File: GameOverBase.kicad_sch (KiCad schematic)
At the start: 51 parts, among them J1 USB_C_Receptacle_USB2.0, J2 Serial Port, J3 add-on conn, Q1 PMN48XP, SW1 SW_DIP_x08, SW2 boot, SW3 Reset, U1 ESP32-WROOM-E, U2 4021, U3 MCP73831-2ACI-OT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

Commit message: Adds footprint for CTS 219-8LPST DIP switches
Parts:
- SW2, SW3: footprint (none) -> GameOver:TXGA_FFC05036-24SBD113W5M_1x24_P0.50mm_Horizontal
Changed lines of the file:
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@@
       (effects (font (size 1.27 1.27)))
     )
-    (property "Footprint" "" (id 2) (at 224.79 146.05 0)
+    (property "Footprint" "GameOver:TXGA_FFC05036-24SBD113W5M_1x24_P0.50mm_Horizontal" (id 2) (at 224.79 146.05 0)
       (effects (font (size 1.27 1.27)) hide)
     )
@@
       (effects (font (size 1.27 1.27)))
     )
-    (property "Footprint" "" (id 2) (at 207.01 146.05 0)
+    (property "Footprint" "GameOver:TXGA_FFC05036-24SBD113W5M_1x24_P0.50mm_Horizontal" (id 2) (at 207.01 146.05 0)
       (effects (font (size 1.27 1.27)) hide)
     )
@@
     )
     (path "/407d0ffb-4748-48d0-84ea-57fc2a5b2510"
-      (reference "SW1") (unit 1) (value "SW_DIP_x08") (footprint "")
+      (reference "SW1") (unit 1) (value "SW_DIP_x08") (footprint "GameOver:DIP-16_CTS_219-8LPST")
     )
     (path "/fbfbda5b-3f1a-4559-9c00-adeb4e1f53ab"

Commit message: Fixes footprint association for both tactile switches
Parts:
- SW1: footprint (none) -> GameOver:DIP-16_CTS_219-8LPST
- SW2, SW3: footprint GameOver:TXGA_FFC05036-24SBD113W5M_1x24_P0.50mm_Horizontal -> (none)
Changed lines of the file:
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@@
       (effects (font (size 1.27 1.27)))
     )
-    (property "Footprint" "GameOver:TXGA_FFC05036-24SBD113W5M_1x24_P0.50mm_Horizontal" (id 2) (at 224.79 146.05 0)
+    (property "Footprint" "" (id 2) (at 224.79 146.05 0)
       (effects (font (size 1.27 1.27)) hide)
     )
@@
       (effects (font (size 1.27 1.27)))
     )
-    (property "Footprint" "" (id 2) (at 121.92 158.75 0)
+    (property "Footprint" "GameOver:DIP-16_CTS_219-8LPST" (id 2) (at 121.92 158.75 0)
       (effects (font (size 1.27 1.27)) hide)
     )
@@
       (effects (font (size 1.27 1.27)))
     )
-    (property "Footprint" "GameOver:TXGA_FFC05036-24SBD113W5M_1x24_P0.50mm_Horizontal" (id 2) (at 207.01 146.05 0)
+    (property "Footprint" "" (id 2) (at 207.01 146.05 0)
       (effects (font (size 1.27 1.27)) hide)
     )
@@
     )
     (path "/fbfbda5b-3f1a-4559-9c00-adeb4e1f53ab"
-      (reference "SW2") (unit 1) (value "boot") (footprint "GameOver:TXGA_FFC05036-24SBD113W5M_1x24_P0.50mm_Horizontal")
+      (reference "SW2") (unit 1) (value "boot") (footprint "GameOver:SW_Tactile_SPST_SOFNG_TS-1814")
     )
     (path "/127be547-9fbb-4f55-a1d1-e12de114ea72"
-      (reference "SW3") (unit 1) (value "Reset") (footprint "GameOver:TXGA_FFC05036-24SBD113W5M_1x24_P0.50mm_Horizontal")
+      (reference "SW3") (unit 1) (value "Reset") (footprint "GameOver:SW_Tactile_SPST_SOFNG_TS-1814")
     )
     (path "/7e6285e9-8fc0-49bf-b49b-a6df46890238"

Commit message: Uses tag-connect TC2030-FP footprint for serial connection to uC
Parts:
- SW2, SW3: footprint (none) -> GameOver:SW_Tactile_SPST_SOFNG_TS-1814
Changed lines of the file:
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@@
       (effects (font (size 1.27 1.27)))
     )
-    (property "Footprint" "" (id 2) (at 224.79 146.05 0)
+    (property "Footprint" "GameOver:SW_Tactile_SPST_SOFNG_TS-1814" (id 2) (at 224.79 146.05 0)
       (effects (font (size 1.27 1.27)) hide)
     )
@@
       (effects (font (size 1.27 1.27)))
     )
-    (property "Footprint" "" (id 2) (at 207.01 146.05 0)
+    (property "Footprint" "GameOver:SW_Tactile_SPST_SOFNG_TS-1814" (id 2) (at 207.01 146.05 0)
       (effects (font (size 1.27 1.27)) hide)
     )
@@
     )
     (path "/a4a4a9b2-b00e-4de8-947c-82cb95b02a26"
-      (reference "J2") (unit 1) (value "Serial Port") (footprint "")
+      (reference "J2") (unit 1) (value "Serial Port") (footprint "Connector:Tag-Connect_TC2030-IDC-FP_2x03_P1.27mm_Vertical")
     )
     (path "/b96389fd-4b84-4e6a-b451-5d6147af997a"

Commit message: Fixes footprint for 4021B
It actually uses TSSOP16 without thermal pads
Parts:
- J2: footprint (none) -> Connector:Tag-Connect_TC2030-IDC-FP_2x03_P1.27mm_Vertical
- U2: footprint Package_SO:TSSOP-16-1EP_4.4x5mm_P0.65mm -> (none)
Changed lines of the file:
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@@
       (effects (font (size 1.27 1.27)) (justify left))
     )
-    (property "Footprint" "Package_SO:TSSOP-16-1EP_4.4x5mm_P0.65mm" (id 2) (at 165.1 147.32 0)
+    (property "Footprint" "" (id 2) (at 165.1 147.32 0)
       (effects (font (size 1.27 1.27)) hide)
     )
@@
       (effects (font (size 1.27 1.27)))
     )
-    (property "Footprint" "" (id 2) (at 49.53 179.07 0)
+    (property "Footprint" "Connector:Tag-Connect_TC2030-IDC-FP_2x03_P1.27mm_Vertical" (id 2) (at 49.53 179.07 0)
       (effects (font (size 1.27 1.27)) hide)
     )
@@
     )
     (path "/317e242a-fc94-41fd-8e86-30d2c1650759"
-      (reference "U2") (unit 1) (value "4021") (footprint "Package_SO:TSSOP-16-1EP_4.4x5mm_P0.65mm")
+      (reference "U2") (unit 1) (value "4021") (footprint "Package_SO:TSSOP-16_4.4x5mm_P0.65mm")
     )
     (path "/e16932c6-4644-4ca2-b59a-6a89b09e35e0"

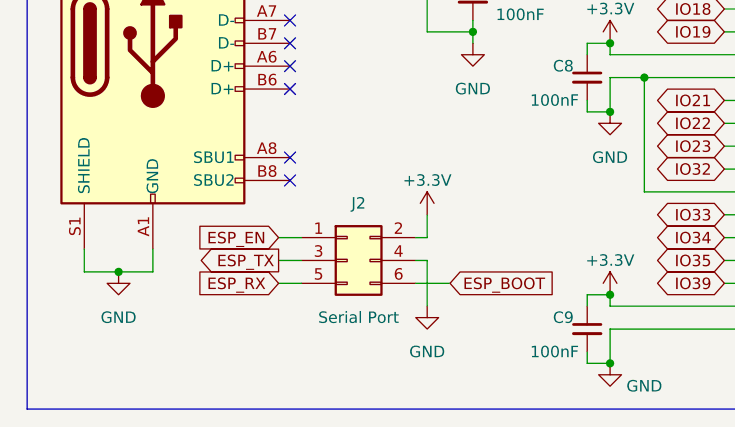
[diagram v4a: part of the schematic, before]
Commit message: Adds solder jumpers to the TX/RX lines
This will make it easier to bodge the PCB in case we mix the lines up.
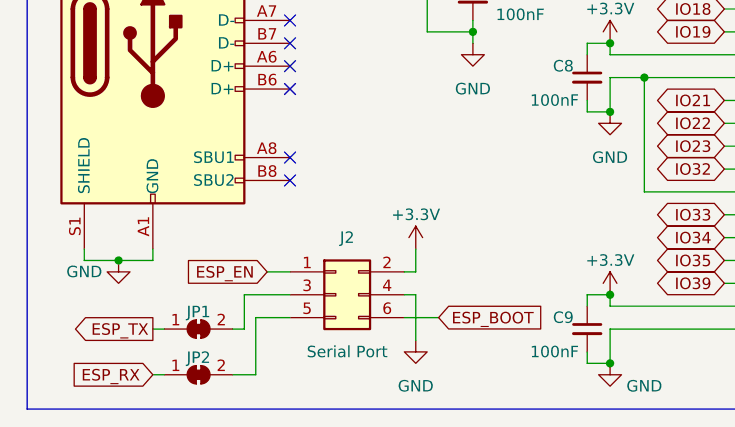
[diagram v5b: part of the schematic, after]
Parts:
- added JP1: (no value), symbol Jumper:SolderJumper_2_Bridged
- added JP2: ~, symbol Jumper:SolderJumper_2_Bridged
- U2: footprint (none) -> Package_SO:TSSOP-16_4.4x5mm_P0.65mm
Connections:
- net ESP_RX: now also JP2.1 (A); no longer J2.5 (Pin_5)
- net ESP_TX: now also JP1.1 (A); no longer J2.3 (Pin_3)
- new net: J2.3 (Pin_3), JP1.2 (B)
- new net: J2.5 (Pin_5), JP2.2 (B)
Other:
- moved on the sheet: J2

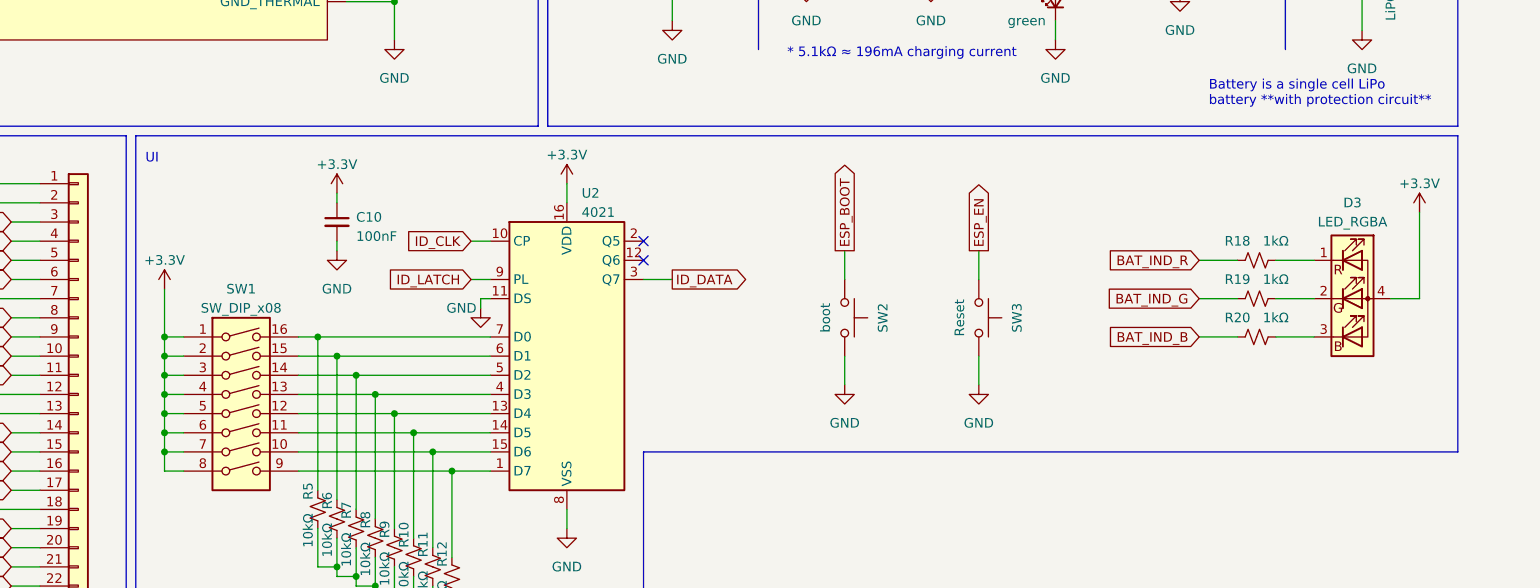
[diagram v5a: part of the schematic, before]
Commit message: Adds two mouting holes for mechanically mounting the PCB onto the case
I used M3 screws because they are much easier to find, but if this
proves too big for the PCB, we can change them to M2.
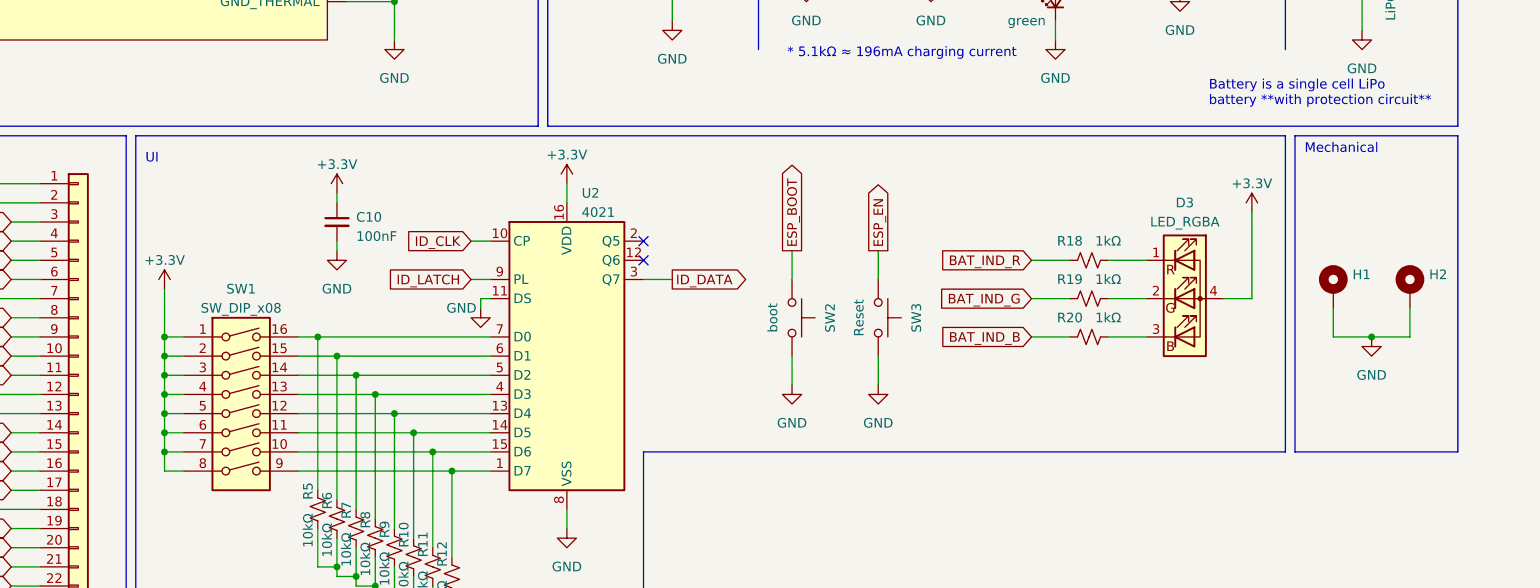
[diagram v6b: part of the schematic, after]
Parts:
- added H1, H2: ~, symbol Mechanical:MountingHole_Pad
- JP1: value (none) -> ~
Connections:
- net GND: now also H1.1, H2.1
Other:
- note added: "Mechanical"
- moved on the sheet: D3, R18, R19, R20, SW2, SW3

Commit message: Assigns footprints that were missing for the solder jumpers in TX/RX lines
These were added in c98b2485 but I forgot to assign a footprint to them.
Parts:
- H1, H2: footprint (none) -> MountingHole:MountingHole_3.2mm_M3_DIN965_Pad
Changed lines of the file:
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@@
       (effects (font (size 1.27 1.27)) (justify left))
     )
-    (property "Footprint" "" (id 2) (at 276.86 142.24 0)
+    (property "Footprint" "MountingHole:MountingHole_3.2mm_M3_DIN965_Pad" (id 2) (at 276.86 142.24 0)
       (effects (font (size 1.27 1.27)) hide)
     )
@@
       (effects (font (size 1.27 1.27)) (justify left))
     )
-    (property "Footprint" "" (id 2) (at 266.7 142.24 0)
+    (property "Footprint" "MountingHole:MountingHole_3.2mm_M3_DIN965_Pad" (id 2) (at 266.7 142.24 0)
       (effects (font (size 1.27 1.27)) hide)
     )
@@
     )
     (path "/153b872c-6c65-47b8-a7a9-c495d607d48b"
-      (reference "JP1") (unit 1) (value "~") (footprint "")
+      (reference "JP1") (unit 1) (value "~") (footprint "Jumper:SolderJumper-2_P1.3mm_Bridged_RoundedPad1.0x1.5mm")
     )
     (path "/c3e79e6e-1418-4802-9ff4-ff4989c54127"
-      (reference "JP2") (unit 1) (value "~") (footprint "")
+      (reference "JP2") (unit 1) (value "~") (footprint "Jumper:SolderJumper-2_P1.3mm_Bridged_RoundedPad1.0x1.5mm")
     )
     (path "/7812657a-77a5-4738-bb49-ebee91b9814f"

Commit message: Creates specific symbol for the DEALON USB-US31-106 USB-C connector
This connector has only a subset of the pins necessary for USB-C for
power only, so we need a specific symbol for it, since the footprint
will not include all the usual USB-C pins.
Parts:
- removed J1: USB_C_Receptacle_USB2.0, GameOver:DEALON_USB-US31-106, symbol Connector:USB_C_Receptacle_USB2.0
- added J1: USB_C_DEALON-USB-US31-106, GameOver:DEALON_USB-US31-106, symbol GameOver:USB_C_DEALON-USB-US31-106
- JP1, JP2: footprint (none) -> Jumper:SolderJumper-2_P1.3mm_Bridged_RoundedPad1.0x1.5mm
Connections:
- net GND: now also J1.A12 (GND), J1.B12 (GND), J1.S1 (SHIELD)
- net at R4.1: now also J1.B5 (CC2)
- net at C6.1, F1.1: now also J1.A9 (VBUS), J1.B9 (VBUS)
- net at R3.1: now also J1.A5 (CC1)
- no-connect marks 8 -> 2
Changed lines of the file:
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@@
   (junction (at 139.7 181.61) (diameter 0) (color 0 0 0 0)
   )
-  (no_connect (at 43.18 152.4))
-  (no_connect (at 43.18 154.94))
-  (no_connect (at 43.18 157.48))
-  (no_connect (at 43.18 160.02))
   (no_connect (at 175.26 138.43))
   (no_connect (at 175.26 135.89))
-  (no_connect (at 43.18 170.18))
-  (no_connect (at 43.18 167.64))
   (wire (pts (xy 26.67 54.61) (xy 29.21 54.61))
     (stroke (width 0) (type default))
@@
       (effects (font (size 1.27 1.27)))
     )
-    (property "Footprint" "" (id 2) (at 33.02 186.69 0)
+    (property "Footprint" "Jumper:SolderJumper-2_P1.3mm_Bridged_RoundedPad1.0x1.5mm" (id 2) (at 33.02 186.69 0)
       (effects (font (size 1.27 1.27)) hide)
     )
@@
     (pin "2")
   )
-  (symbol (lib_id "Connector:USB_C_Receptacle_USB2.0") (at 27.94 154.94 0) (unit 1)
-    (in_bom yes) (on_board yes) (fields_autoplaced)
-    (property "Reference" "J1" (id 0) (at 27.94 133.35 0)
-      (effects (font (size 1.27 1.27)))
-    )
-    (property "Value" "USB_C_Receptacle_USB2.0" (id 1) (at 27.94 135.89 0)
-      (effects (font (size 1.27 1.27)))
-    )
-    (property "Footprint" "GameOver:DEALON_USB-US31-106" (id 2) (at 31.75 154.94 0)
-      (effects (font (size 1.27 1.27)) hide)
-    )
-    (property "Datasheet" "https://www.usb.org/sites/default/files/documents/usb_type-c.zip" (id 3) (at 31.75 154.94 0)
-      (effects (font (size 1.27 1.27)) hide)
-    )
-    (pin "A1")
-    (pin "A12")
-    (pin "A4")
-    (pin "A5")
-    (pin "A6")
-    (pin "A7")
-    (pin "A8")
-    (pin "A9")
-    (pin "B1")
-    (pin "B12")
-    (pin "B4")
-    (pin "B5")
-    (pin "B6")
-    (pin "B7")
-    (pin "B8")
-    (pin "B9")
-    (pin "S1")
-  )
   (symbol (lib_id "Device:C_Small") (at 241.3 96.52 0) (unit 1)
     (in_bom yes) (on_board yes) (fields_autoplaced)
@@
       (effects (font (size 1.27 1.27)))
     )
-    (property "Footprint" "" (id 2) (at 33.02 191.77 0)
+    (property "Footprint" "Jumper:SolderJumper-2_P1.3mm_Bridged_RoundedPad1.0x1.5mm" (id 2) (at 33.02 191.77 0)
       (effects (font (size 1.27 1.27)) hide)
     )
@@
     (pin "2")
   )
+  (symbol (lib_id "GameOver:USB_C_DEALON-USB-US31-106") (at 27.94 154.94 0) (unit 1)
+    (in_bom yes) (on_board yes)
+    (property "Reference" "J1" (id 0) (at 27.94 133.35 0)
+      (effects (font (size 1.27 1.27)))
+    )
+    (property "Value" "USB_C_DEALON-USB-US31-106" (id 1) (at 30.48 135.89 0)
+      (effects (font (size 1.27 1.27)))
+    )
+    (property "Footprint" "GameOver:DEALON_USB-US31-106" (id 2) (at 31.75 154.94 0)
+      (effects (font (size 1.27 1.27)) hide)
+    )
+    (property "Datasheet" "https://www.usb.org/sites/default/files/documents/usb_type-c.zip" (id 3) (at 31.75 154.94 0)
+      (effects (font (size 1.27 1.27)) hide)
+    )
+    (pin "A12")
+    (pin "A5")
+    (pin "A9")
+    (pin "B12")
+    (pin "B5")
+    (pin "B9")
+    (pin "S1")
+  )
   (symbol (lib_id "Device:R_Small_US") (at 144.78 177.8 0) (unit 1)
     (in_bom yes) (on_board yes)
@@
       (reference "H2") (unit 1) (value "~") (footprint "MountingHole:MountingHole_3.2mm_M3_DIN965_Pad")
     )
-    (path "/60060b39-57f0-4f2c-a062-c391396cf2bf"
-      (reference "J1") (unit 1) (value "USB_C_Receptacle_USB2.0") (footprint "GameOver:DEALON_USB-US31-106")
+    (path "/c62df308-9d46-4880-b5c7-5b78f375875b"
+      (reference "J1") (unit 1) (value "USB_C_DEALON-USB-US31-106") (footprint "GameOver:DEALON_USB-US31-106")
     )
     (path "/a4a4a9b2-b00e-4de8-947c-82cb95b02a26"
